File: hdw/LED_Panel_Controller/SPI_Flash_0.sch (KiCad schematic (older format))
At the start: 14 parts

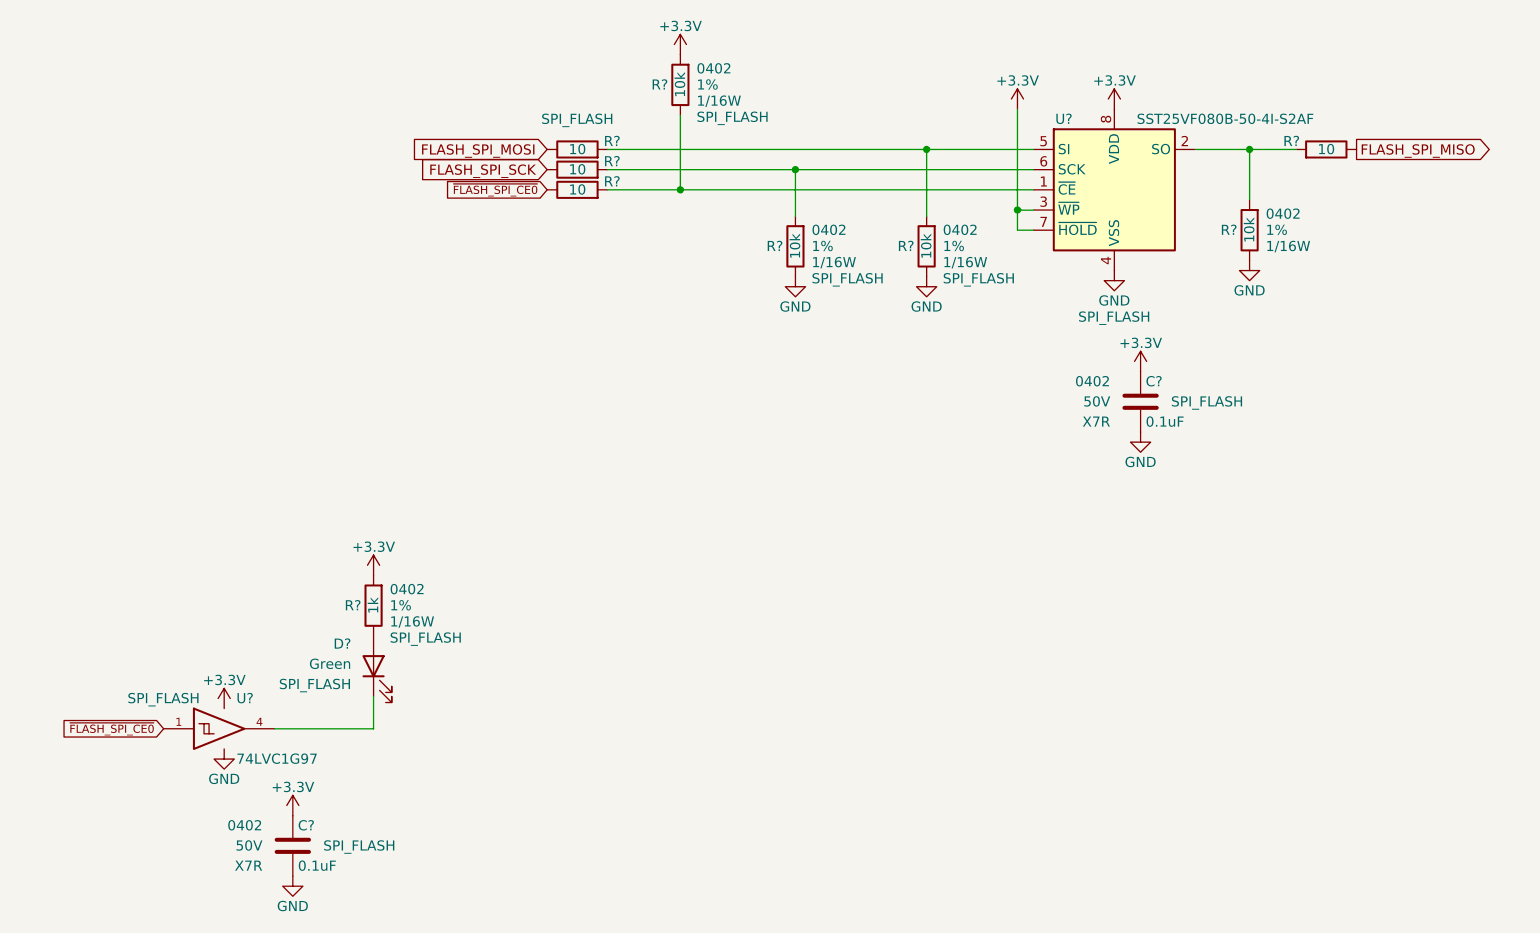
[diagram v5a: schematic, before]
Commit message: assigned I2C addresses
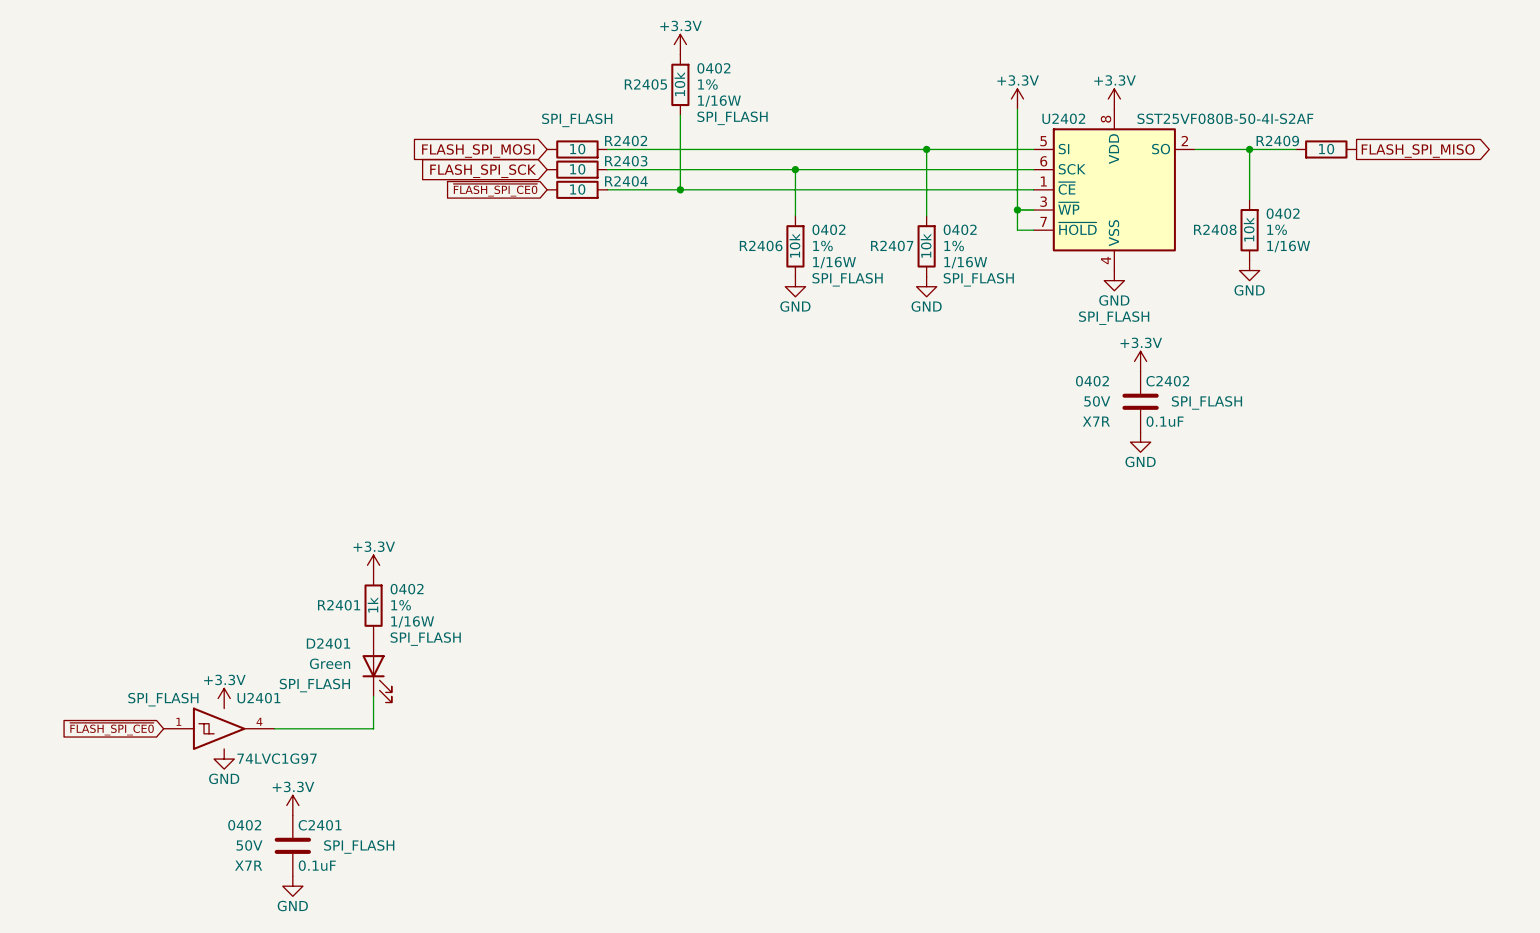
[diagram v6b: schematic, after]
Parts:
- removed C? (x2): 0.1uF, Capacitors_SMD:C_0402, symbol Custom_Library:C_Custom
- removed D?: Green, LEDs:LED_0402, symbol Device:LED
- removed R? (x4): 10k, Resistors_SMD:R_0402, symbol Custom_Library:R_Custom
- removed R? (x4): 10, Resistors_SMD:R_0402, symbol Custom_Library:R_Custom
- removed R?: 1k, Resistors_SMD:R_0402, symbol Custom_Library:R_Custom
- removed U?: SST25VF080B-50-4I-S2AF, Package_SO:SOIC-8_5.275x5.275mm_P1.27mm, symbol Memory_Flash:SST25VF080B-50-4x-S2Ax
- added C2401, C2402: 0.1uF, Capacitors_SMD:C_0402, symbol Custom_Library:C_Custom
- added D2401: Green, LEDs:LED_0402, symbol Device:LED
- added R2401: 1k, Resistors_SMD:R_0402, symbol Custom_Library:R_Custom
- added R2402, R2403, R2404, R2409: 10, Resistors_SMD:R_0402, symbol Custom_Library:R_Custom
- added R2405, R2406, R2407, R2408: 10k, Resistors_SMD:R_0402, symbol Custom_Library:R_Custom
- added U2402: SST25VF080B-50-4I-S2AF, Package_SO:SOIC-8_5.275x5.275mm_P1.27mm, symbol Memory_Flash:SST25VF080B-50-4x-S2Ax
- gave numbers to parts that had none: 1
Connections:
- net +3V3: now also C2401.1, C2402.1, R2401.1, R2405.1, U2402.3 (~WP~), U2402.7 (~HOLD~), U2402.8 (VDD)
- net FLASH_SPI_MISO: now also R2409.2
- net FLASH_SPI_MOSI: now also R2402.2
- net FLASH_SPI_SCK: now also R2403.2
- net GND: now also C2401.2, C2402.2, R2406.2, R2407.2, R2408.2, U2402.4 (VSS)
- net ~FLASH_SPI_CE0: now also R2404.2
- net at U2401.4: now also D2401.1 (K)
- new net: R2408.1, R2409.1, U2402.2 (SO)
- new net: R2402.1, R2407.1, U2402.5 (SI)
- new net: D2401.2 (A), R2401.2
- new net: R2404.1, R2405.2, U2402.1 (~CE)
- new net: R2403.1, R2406.1, U2402.6 (SCK)
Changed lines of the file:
@@
 $EndDescr
 $Comp
-L power:GND #PWR?
-U 1 1 5BB4E0E3
+L power:GND #PWR02411
+U 1 1 6078625F
 P 6080 4050
-F 0 "#PWR?" H 6080 3800 50  0001 C CNN
+F 0 "#PWR02411" H 6080 3800 50  0001 C CNN
 F 1 "GND" H 6080 3900 50  0000 C CNN
 F 2 "" H 6080 4050 50  0001 C CNN
@@
 $EndComp
 $Comp
-L Custom_Library:R_Custom R?
-U 1 1 5BB4EDD1
+L Custom_Library:R_Custom R2408
+U 1 1 60786269
 P 6750 3850
-F 0 "R?" H 6690 3850 50  0000 R CNN
+F 0 "R2408" H 6690 3850 50  0000 R CNN
 F 1 "10k" V 6750 3850 50  0000 C CNN
 F 2 "Resistors_SMD:R_0402" H 6750 3850 50  0001 C CNN
@@
 $EndComp
 $Comp
-L power:GND #PWR?
-U 1 1 5BB4EE63
+L power:GND #PWR02408
+U 1 1 6078626F
 P 5150 4080
-F 0 "#PWR?" H 5150 3830 50  0001 C CNN
+F 0 "#PWR02408" H 5150 3830 50  0001 C CNN
 F 1 "GND" H 5150 3930 50  0000 C CNN
 F 2 "" H 5150 4080 50  0001 C CNN
@@
 $EndComp
 $Comp
-L power:GND #PWR?
-U 1 1 5BB4EE7C
+L power:GND #PWR02414
+U 1 1 60786278
 P 6750 4000
-F 0 "#PWR?" H 6750 3750 50  0001 C CNN
+F 0 "#PWR02414" H 6750 3750 50  0001 C CNN
 F 1 "GND" H 6750 3850 50  0000 C CNN
 F 2 "" H 6750 4000 50  0001 C CNN
@@
 $EndComp
 $Comp
-L Custom_Library:R_Custom R?
-U 1 1 5BB4F53B
+L Custom_Library:R_Custom R2402
+U 1 1 6078627D
 P 3420 3450
-F 0 "R?" V 3380 3580 50  0000 L CNN
+F 0 "R2402" V 3380 3580 50  0000 L CNN
 F 1 "10" V 3420 3450 50  0000 C CNN
 F 2 "Resistors_SMD:R_0402" H 3420 3450 50  0001 C CNN
@@
 	3570 3650 3930 3650
 $Comp
-L power:+3.3V #PWR?
+L power:+3.3V #PWR02406
 U 1 1 5BDF3D33
 P 3930 2980
-F 0 "#PWR?" H 3930 2830 50  0001 C CNN
+F 0 "#PWR02406" H 3930 2830 50  0001 C CNN
 F 1 "+3.3V" H 3930 3120 50  0000 C CNN
 F 2 "" H 3930 2980 50  0001 C CNN
@@
 $EndComp
 $Comp
-L power:+3.3V #PWR?
-U 1 1 5BDF3DF4
+L power:+3.3V #PWR02410
+U 1 1 6078628B
 P 6080 3250
-F 0 "#PWR?" H 6080 3100 50  0001 C CNN
+F 0 "#PWR02410" H 6080 3100 50  0001 C CNN
 F 1 "+3.3V" H 6080 3390 50  0000 C CNN
 F 2 "" H 6080 3250 50  0001 C CNN
@@
 $Comp
 L Custom_Library:C_Custom C?
-U 1 1 5C15F697
+U 1 1 60786290
 P 2010 6900
-AR Path="/5BAAE16C/5C15F697" Ref="C?"  Part="1"
-AR Path="/5BB181D8/5C15F697" Ref="C?"  Part="1"
-AR Path="/5BB2595E/5C15F697" Ref="C?"  Part="1"
-AR Path="/5F583577/5C15F697" Ref="C?"  Part="1"
-F 0 "C?" H 2035 7000 50  0000 L CNN
+AR Path="/5BAAE16C/60786290" Ref="C?"  Part="1"
+AR Path="/5BB181D8/60786290" Ref="C?"  Part="1"
+AR Path="/5BB2595E/60786290" Ref="C?"  Part="1"
+AR Path="/5F583577/60786290" Ref="C2401"  Part="1"
+F 0 "C2401" H 2035 7000 50  0000 L CNN
 F 1 "0.1uF" H 2035 6800 50  0000 L CNN
 F 2 "Capacitors_SMD:C_0402" H 2048 6750 50  0001 C CNN
@@
 $EndComp
 $Comp
-L power:+3.3V #PWR?
-U 1 1 5C161B83
+L power:+3.3V #PWR02401
+U 1 1 60786299
 P 1670 6220
-F 0 "#PWR?" H 1670 6070 50  0001 C CNN
+F 0 "#PWR02401" H 1670 6070 50  0001 C CNN
 F 1 "+3.3V" H 1670 6360 50  0000 C CNN
 F 2 "" H 1670 6220 50  0001 C CNN
@@
 $EndComp
 $Comp
-L power:+3.3V #PWR?
+L power:+3.3V #PWR02403
 U 1 1 5C161BE9
 P 2010 6750
-F 0 "#PWR?" H 2010 6600 50  0001 C CNN
+F 0 "#PWR02403" H 2010 6600 50  0001 C CNN
 F 1 "+3.3V" H 2010 6890 50  0000 C CNN
 F 2 "" H 2010 6750 50  0001 C CNN
@@
 $EndComp
 $Comp
-L power:GND #PWR?
-U 1 1 5C161C44
+L power:GND #PWR02404
+U 1 1 607862A9
 P 2010 7050
-F 0 "#PWR?" H 2010 6800 50  0001 C CNN
+F 0 "#PWR02404" H 2010 6800 50  0001 C CNN
 F 1 "GND" H 2010 6900 50  0000 C CNN
 F 2 "" H 2010 7050 50  0001 C CNN
@@
 $EndComp
 $Comp
-L power:GND #PWR?
-U 1 1 5C161C9F
+L power:GND #PWR02402
+U 1 1 607862AE
 P 1670 6420
-F 0 "#PWR?" H 1670 6170 50  0001 C CNN
+F 0 "#PWR02402" H 1670 6170 50  0001 C CNN
 F 1 "GND" H 1670 6270 50  0000 C CNN
 F 2 "" H 1670 6420 50  0001 C CNN
@@
 AR Path="/5BF346B3/5C166A81" Ref="#PWR?"  Part="1"
 AR Path="/5BB2595E/5C166A81" Ref="#PWR?"  Part="1"
-AR Path="/5F583577/5C166A81" Ref="#PWR?"  Part="1"
-F 0 "#PWR?" H 2410 5410 50  0001 C CNN
+AR Path="/5F583577/5C166A81" Ref="#PWR02405"  Part="1"
+F 0 "#PWR02405" H 2410 5410 50  0001 C CNN
 F 1 "+3.3V" H 2410 5700 50  0000 C CNN
 F 2 "" H 2410 5560 50  0001 C CNN
@@
 $Comp
 L Device:LED D?
-U 1 1 5C166A95
+U 1 1 607862BE
 P 2410 6010
-AR Path="/5BB844FD/5C166A95" Ref="D?"  Part="1"
-AR Path="/5BF346B3/5C166A95" Ref="D?"  Part="1"
-AR Path="/5BB2595E/5C166A95" Ref="D?"  Part="1"
-AR Path="/5F583577/5C166A95" Ref="D?"  Part="1"
-F 0 "D?" V 2520 6120 50  0000 L CNN
+AR Path="/5BB844FD/607862BE" Ref="D?"  Part="1"
+AR Path="/5BF346B3/607862BE" Ref="D?"  Part="1"
+AR Path="/5BB2595E/607862BE" Ref="D?"  Part="1"
+AR Path="/5F583577/607862BE" Ref="D2401"  Part="1"
+F 0 "D2401" V 2520 6120 50  0000 L CNN
 F 1 "Green" V 2420 6120 50  0000 L CNN
 F 2 "LEDs:LED_0402" H 2410 6010 50  0001 C CNN
@@
 $EndComp
 $Comp
-L Memory_Flash:SST25VF080B-50-4x-S2Ax U?
-U 1 1 5F6879D5
+L Memory_Flash:SST25VF080B-50-4x-S2Ax U2402
+U 1 1 607862FC
 P 6080 3650
-F 0 "U?" H 5830 4000 50  0000 C CNN
+F 0 "U2402" H 5830 4000 50  0000 C CNN
 F 1 "SST25VF080B-50-4I-S2AF" H 6630 4000 50  0000 C CNN
 F 2 "Package_SO:SOIC-8_5.275x5.275mm_P1.27mm" H 6080 2950 50  0001 C CNN
@@
 $EndComp
 $Comp
-L power:+3.3V #PWR?
+L power:+3.3V #PWR02412
 U 1 1 5F689292
 P 6210 4550
-F 0 "#PWR?" H 6210 4400 50  0001 C CNN
+F 0 "#PWR02412" H 6210 4400 50  0001 C CNN
 F 1 "+3.3V" H 6210 4690 50  0000 C CNN
 F 2 "" H 6210 4550 50  0001 C CNN
@@
 $EndComp
 $Comp
-L power:GND #PWR?
-U 1 1 5F689298
+L power:GND #PWR02413
+U 1 1 60786306
 P 6210 4850
-F 0 "#PWR?" H 6210 4600 50  0001 C CNN
+F 0 "#PWR02413" H 6210 4600 50  0001 C CNN
 F 1 "GND" H 6210 4700 50  0000 C CNN
 F 2 "" H 6210 4850 50  0001 C CNN
@@
 $EndComp
 $Comp
-L power:+3.3V #PWR?
-U 1 1 5F69329F
+L power:+3.3V #PWR02409
+U 1 1 60786311
 P 5600 3250
-F 0 "#PWR?" H 5600 3100 50  0001 C CNN
+F 0 "#PWR02409" H 5600 3100 50  0001 C CNN
 F 1 "+3.3V" H 5600 3390 50  0000 C CNN
 F 2 "" H 5600 3250 50  0001 C CNN
@@
 	3570 3550 4500 3550
 $Comp
-L Custom_Library:R_Custom R?
-U 1 1 5F697048
+L Custom_Library:R_Custom R2406
+U 1 1 60786314
 P 4500 3930
-F 0 "R?" H 4440 3930 50  0000 R CNN
+F 0 "R2406" H 4440 3930 50  0000 R CNN
 F 1 "10k" V 4500 3930 50  0000 C CNN
 F 2 "Resistors_SMD:R_0402" H 4500 3930 50  0001 C CNN
@@
 $EndComp
 $Comp
-L power:GND #PWR?
-U 1 1 5F697052
+L power:GND #PWR02407
+U 1 1 60786319
 P 4500 4080
-F 0 "#PWR?" H 4500 3830 50  0001 C CNN
+F 0 "#PWR02407" H 4500 3830 50  0001 C CNN
 F 1 "GND" H 4500 3930 50  0000 C CNN
 F 2 "" H 4500 4080 50  0001 C CNN
@@
 	4500 3550 5680 3550
 $Comp
-L Custom_Library:R_Custom R?
-U 1 1 5F7379BB
+L Custom_Library:R_Custom R2403
+U 1 1 60786321
 P 3420 3550
-F 0 "R?" V 3380 3680 50  0000 L CNN
+F 0 "R2403" V 3380 3680 50  0000 L CNN
 F 1 "10" V 3420 3550 50  0000 C CNN
 F 2 "Resistors_SMD:R_0402" H 3420 3550 50  0001 C CNN
@@
 $EndComp
 $Comp
-L Custom_Library:R_Custom R?
-U 1 1 5F737B74
+L Custom_Library:R_Custom R2404
+U 1 1 6078632A
 P 3420 3650
-F 0 "R?" V 3380 3780 50  0000 L CNN
+F 0 "R2404" V 3380 3780 50  0000 L CNN
 F 1 "10" V 3420 3650 50  0000 C CNN
 F 2 "Resistors_SMD:R_0402" H 3420 3650 50  0001 C CNN
@@
 $EndComp
 $Comp
-L Custom_Library:R_Custom R?
-U 1 1 5F737D15
+L Custom_Library:R_Custom R2409
+U 1 1 6078632E
 P 7130 3450
-F 0 "R?" V 7090 3580 50  0000 L CNN
+F 0 "R2409" V 7090 3580 50  0000 L CNN
 F 1 "10" V 7130 3450 50  0000 C CNN
 F 2 "Resistors_SMD:R_0402" H 7130 3450 50  0001 C CNN
@@
 $EndComp
 $Comp
-L Custom_Library:74LVC1G97_Power_BUF U?
+L Custom_Library:74LVC1G97_Power_BUF U2401
 U 1 1 5FE9D8D5
 P 1670 6320
-F 0 "U?" H 1730 6470 50  0000 L CNN
+F 0 "U2401" H 1730 6470 50  0000 L CNN
 F 1 "74LVC1G97" H 1730 6170 50  0000 L CNN
 F 2 "Package_TO_SOT_SMD:SOT-363_SC-70-6" H 1720 6320 50  0001 C CNN
@@
 $EndComp
 $Comp
-L Custom_Library:R_Custom R?
-U 1 1 6026393A
+L Custom_Library:R_Custom R2407
+U 1 1 60786355
 P 5150 3930
-F 0 "R?" H 5090 3930 50  0000 R CNN
+F 0 "R2407" H 5090 3930 50  0000 R CNN
 F 1 "10k" V 5150 3930 50  0000 C CNN
 F 2 "Resistors_SMD:R_0402" H 5150 3930 50  0001 C CNN
@@
 $EndComp
 $Comp
-L Custom_Library:R_Custom R?
-U 1 1 60263FB7
+L Custom_Library:R_Custom R2405
+U 1 1 60786360
 P 3930 3130
-F 0 "R?" H 3870 3130 50  0000 R CNN
+F 0 "R2405" H 3870 3130 50  0000 R CNN
 F 1 "10k" V 3930 3130 50  0000 C CNN
 F 2 "Resistors_SMD:R_0402" H 3930 3130 50  0001 C CNN
@@
 $EndComp
 $Comp
-L Custom_Library:R_Custom R?
-U 1 1 60266213
+L Custom_Library:R_Custom R2401
+U 1 1 60786368
 P 2410 5710
-F 0 "R?" H 2350 5710 50  0000 R CNN
+F 0 "R2401" H 2350 5710 50  0000 R CNN
 F 1 "1k" V 2410 5710 50  0000 C CNN
 F 2 "Resistors_SMD:R_0402" H 2410 5710 50  0001 C CNN
@@
 $Comp
 L Custom_Library:C_Custom C?
-U 1 1 60269564
+U 1 1 6078636C
 P 6210 4700
-AR Path="/5BAAE16C/60269564" Ref="C?"  Part="1"
-AR Path="/5BB181D8/60269564" Ref="C?"  Part="1"
-AR Path="/5BB2595E/60269564" Ref="C?"  Part="1"
-AR Path="/5F583577/60269564" Ref="C?"  Part="1"
-F 0 "C?" H 6235 4800 50  0000 L CNN
+AR Path="/5BAAE16C/6078636C" Ref="C?"  Part="1"
+AR Path="/5BB181D8/6078636C" Ref="C?"  Part="1"
+AR Path="/5BB2595E/6078636C" Ref="C?"  Part="1"
+AR Path="/5F583577/6078636C" Ref="C2402"  Part="1"
+F 0 "C2402" H 6235 4800 50  0000 L CNN
 F 1 "0.1uF" H 6235 4600 50  0000 L CNN
 F 2 "Capacitors_SMD:C_0402" H 6248 4550 50  0001 C CNN
